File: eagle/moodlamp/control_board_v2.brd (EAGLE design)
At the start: 49.5 x 40 mm, 43 parts, among them IC1 MEGA8-AI, J1 POWER_JACKPTH, Q1 N-HEXFET-2D_SOT232-IRLL014N, Q2 N-HEXFET-2D_SOT232-IRLL014N, Q3 N-HEXFET-2D_SOT232-IRLL014N

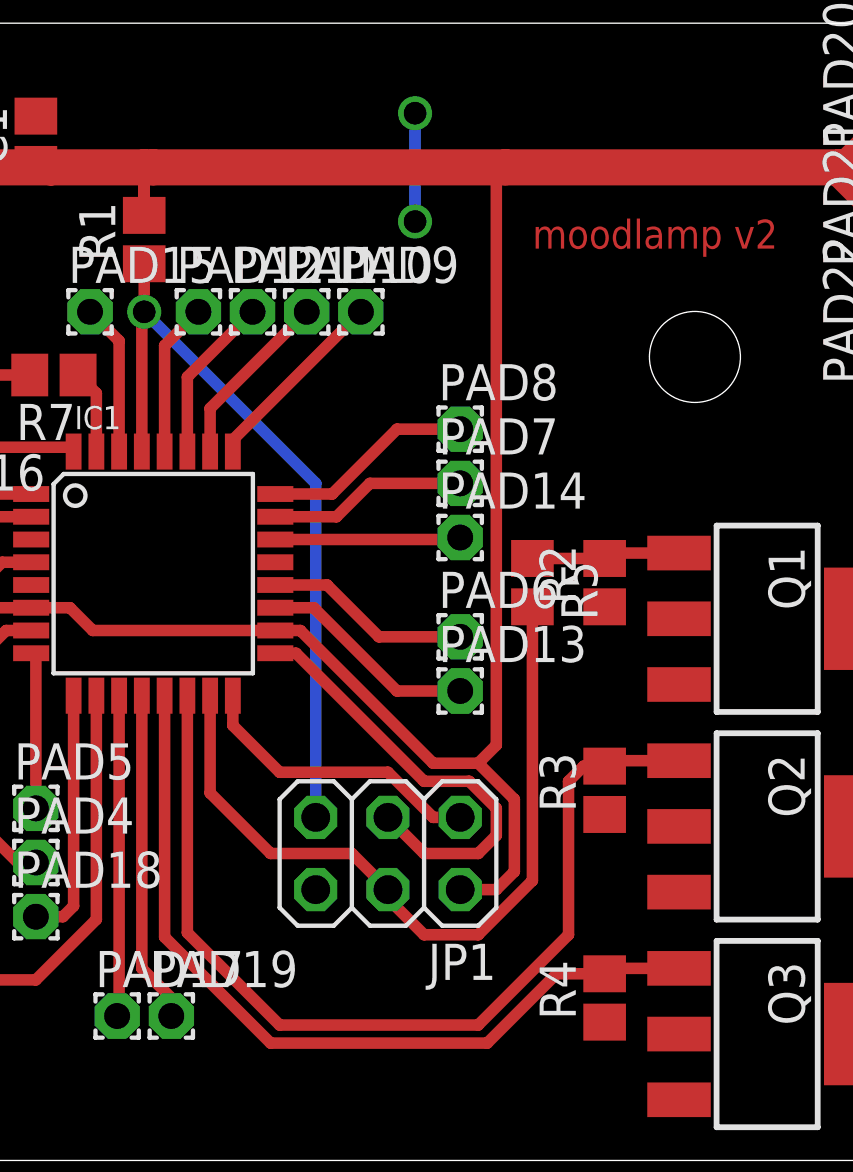
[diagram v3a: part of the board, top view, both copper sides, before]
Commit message: isp connector orientation fixed
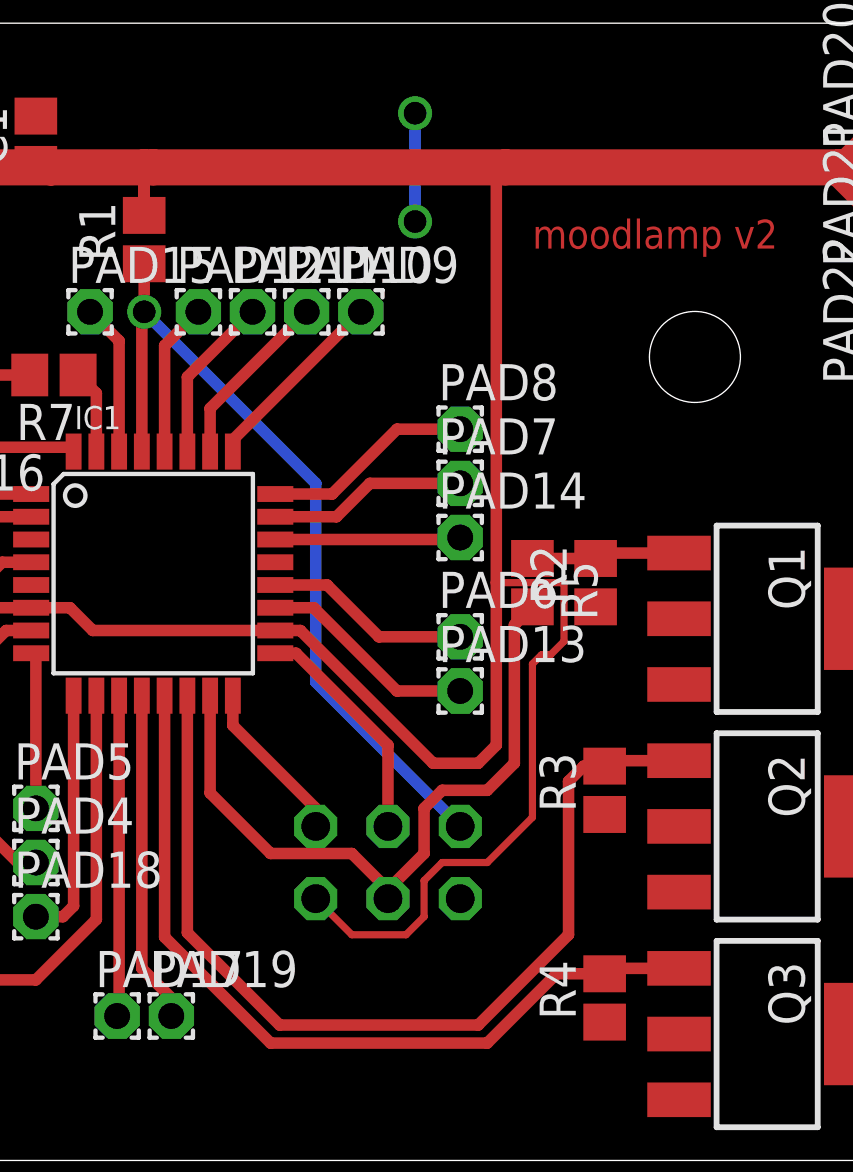
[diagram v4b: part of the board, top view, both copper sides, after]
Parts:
- moved R2 0.32 mm to (35.2, 20.3)
- moved JP1 0.32 mm to (27.9, 10.5), flipped to the bottom
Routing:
- net VCC: track 113.6 -> 129.0 mm
- net N$13: track 15.6 -> 8.16 mm
- net N$1: track 10.4 -> 5.80 mm
- net N$2: track 27.4 -> 24.4 mm
- net RST: track 27.0 -> 29.5 mm
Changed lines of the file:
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@@
 <element name="PAD1" library="wirepad" package="2,54/1,0" value="" x="47.625" y="19.05"/>
 <element name="Q1" library="transistor-power" package="SOT223" value="N-HEXFET-2D_SOT232-IRLL014N" x="41.275" y="19.05" rot="R270"/>
-<element name="R2" library="resistor" package="R0805" value="" x="35.56" y="20.32" rot="R90"/>
+<element name="R2" library="resistor" package="R0805" value="" x="35.2425" y="20.32" rot="R90"/>
 <element name="PAD2" library="wirepad" package="2,54/1,0" value="" x="47.625" y="11.7475"/>
 <element name="Q2" library="transistor-power" package="SOT223" value="N-HEXFET-2D_SOT232-IRLL014N" x="41.275" y="11.7475" rot="R270"/>
@@
 <element name="S2" library="switch" package="SKHMPXE010" value="SKHMPSE010" x="5.715" y="4.1275" rot="R180"/>
 <element name="USB1" library="usb_con-update" package="MOLEX-47364-0001" value="MOLEX-47346-0001" x="1.27" y="20.955"/>
-<element name="JP1" library="pinhead" package="2X03" value="" x="27.94" y="10.795" rot="R180"/>
+<element name="JP1" library="pinhead" package="2X03" value="" x="27.94" y="10.4775" rot="MR180"/>
 <element name="PAD4" library="wirepad" package="1,6/0,9" value="" x="15.5575" y="10.4775"/>
 <element name="PAD5" library="wirepad" package="1,6/0,9" value="" x="15.5575" y="12.3825"/>
@@
 <wire x1="24.86" y1="18.6375" x2="29.5275" y2="13.97" width="0.4064" layer="1"/>
 <wire x1="29.5275" y1="13.97" x2="31.115" y2="13.97" width="0.4064" layer="1"/>
-<wire x1="31.115" y1="13.97" x2="32.385" y2="12.7" width="0.4064" layer="1"/>
-<wire x1="32.385" y1="12.7" x2="32.385" y2="10.16" width="0.4064" layer="1"/>
-<wire x1="32.385" y1="10.16" x2="31.75" y2="9.525" width="0.4064" layer="1"/>
-<wire x1="31.75" y1="9.525" x2="30.48" y2="9.525" width="0.4064" layer="1"/>
 <wire x1="15.3924" y1="19.4375" x2="13.97" y2="19.4375" width="0.4064" layer="1"/>
 <wire x1="13.97" y1="19.4375" x2="13.32125" y2="19.4375" width="0.4064" layer="1"/>
@@
 <wire x1="19.3675" y1="34.925" x2="32.0675" y2="34.925" width="0.4064" layer="1"/>
 <wire x1="32.0675" y1="34.925" x2="31.75" y2="34.6075" width="0.4064" layer="1"/>
-<wire x1="31.75" y1="34.6075" x2="31.75" y2="14.605" width="0.4064" layer="1"/>
+<wire x1="31.75" y1="34.6075" x2="31.75" y2="20.32" width="0.4064" layer="1"/>
+<wire x1="31.75" y1="20.32" x2="31.75" y2="14.605" width="0.4064" layer="1"/>
 <wire x1="31.75" y1="14.605" x2="31.115" y2="13.97" width="0.4064" layer="1"/>
 <wire x1="13.335" y1="34.925" x2="11.1125" y2="32.7025" width="1.27" layer="1"/>
@@
 <wire x1="15.5575" y1="35.0275" x2="16.09" y2="34.925" width="1.27" layer="1"/>
 <wire x1="16.09" y1="34.925" x2="13.335" y2="34.925" width="1.27" layer="1"/>
+<wire x1="33.655" y1="17.78" x2="34.13125" y2="18.25625" width="0.254" layer="1"/>
+<wire x1="34.13125" y1="18.25625" x2="34.13125" y2="20.32" width="0.254" layer="1"/>
+<wire x1="34.13125" y1="20.32" x2="31.75" y2="20.32" width="0.254" layer="1"/>
+<wire x1="33.655" y1="17.78" x2="33.3375" y2="17.78" width="0.254" layer="1"/>
+<wire x1="33.3375" y1="17.78" x2="33.02" y2="17.4625" width="0.254" layer="1"/>
+<wire x1="33.02" y1="17.4625" x2="33.02" y2="12.065" width="0.254" layer="1"/>
+<wire x1="33.02" y1="12.065" x2="31.4325" y2="10.4775" width="0.254" layer="1"/>
+<wire x1="31.4325" y1="10.4775" x2="29.845" y2="10.4775" width="0.254" layer="1"/>
+<wire x1="29.845" y1="10.4775" x2="29.21" y2="9.8425" width="0.254" layer="1"/>
+<wire x1="29.21" y1="9.8425" x2="29.21" y2="8.5725" width="0.254" layer="1"/>
+<wire x1="29.21" y1="8.5725" x2="28.575" y2="7.9375" width="0.254" layer="1"/>
+<wire x1="28.575" y1="7.9375" x2="26.67" y2="7.9375" width="0.254" layer="1"/>
+<wire x1="26.67" y1="7.9375" x2="25.4" y2="9.2075" width="0.254" layer="1"/>
 </signal>
 <signal name="RST">
@@
 <contactref element="JP1" pad="5"/>
 <wire x1="19.285" y1="31.4525" x2="19.3675" y2="31.535" width="0.4064" layer="1"/>
-<wire x1="25.4" y1="12.065" x2="25.4" y2="23.8125" width="0.4064" layer="16"/>
 <wire x1="25.4" y1="23.8125" x2="19.3675" y2="29.845" width="0.4064" layer="16"/>
 <via x="19.3675" y="29.845" extent="1-16" drill="0.8"/>
@@
 <wire x1="19.285" y1="24.9301" x2="19.285" y2="29.7625" width="0.4064" layer="1"/>
 <wire x1="19.285" y1="29.7625" x2="19.3675" y2="29.845" width="0.4064" layer="1"/>
+<wire x1="30.48" y1="11.7475" x2="25.4" y2="16.8275" width="0.4064" layer="16"/>
+<wire x1="25.4" y1="16.8275" x2="25.4" y2="23.8125" width="0.4064" layer="16"/>
 </signal>
 <signal name="N$2">
@@
 <contactref element="R5" pad="2"/>
 <contactref element="JP1" pad="4"/>
-<wire x1="33.02" y1="9.8425" x2="33.02" y2="19.47" width="0.4064" layer="1"/>
-<wire x1="27.94" y1="9.525" x2="27.94" y2="9.2075" width="0.4064" layer="1"/>
-<wire x1="27.94" y1="9.2075" x2="29.21" y2="7.9375" width="0.4064" layer="1"/>
-<wire x1="29.21" y1="7.9375" x2="31.115" y2="7.9375" width="0.4064" layer="1"/>
-<wire x1="31.115" y1="7.9375" x2="33.02" y2="9.8425" width="0.4064" layer="1"/>
 <wire x1="23.8125" y1="10.795" x2="26.67" y2="10.795" width="0.4064" layer="1"/>
-<wire x1="26.67" y1="10.795" x2="27.94" y2="9.525" width="0.4064" layer="1"/>
 <wire x1="21.685" y1="16.3449" x2="21.685" y2="12.9225" width="0.4064" layer="1"/>
 <wire x1="21.685" y1="12.9225" x2="23.8125" y2="10.795" width="0.4064" layer="1"/>
+<wire x1="26.67" y1="10.795" x2="27.94" y2="9.525" width="0.4064" layer="1"/>
+<wire x1="27.94" y1="9.2075" x2="27.94" y2="9.525" width="0.4064" layer="1"/>
+<wire x1="27.94" y1="9.525" x2="29.21" y2="10.795" width="0.4064" layer="1"/>
+<wire x1="29.21" y1="10.795" x2="29.21" y2="12.3825" width="0.4064" layer="1"/>
+<wire x1="29.21" y1="12.3825" x2="29.845" y2="13.0175" width="0.4064" layer="1"/>
+<wire x1="29.845" y1="13.0175" x2="31.4325" y2="13.0175" width="0.4064" layer="1"/>
+<wire x1="31.4325" y1="13.0175" x2="32.385" y2="13.97" width="0.4064" layer="1"/>
+<wire x1="32.385" y1="13.97" x2="32.385" y2="18.835" width="0.4064" layer="1"/>
+<wire x1="32.385" y1="18.835" x2="33.02" y2="19.47" width="0.4064" layer="1"/>
 </signal>
 <signal name="N$3">
@@
 <contactref element="Q1" pad="1"/>
 <contactref element="R5" pad="1"/>
-<wire x1="33.02" y1="21.17" x2="35.56" y2="21.17" width="0.4064" layer="1"/>
-<wire x1="35.56" y1="21.17" x2="35.751" y2="21.361" width="0.4064" layer="1"/>
+<wire x1="33.02" y1="21.17" x2="35.2425" y2="21.17" width="0.4064" layer="1"/>
+<wire x1="35.2425" y1="21.17" x2="35.751" y2="21.361" width="0.4064" layer="1"/>
 <wire x1="35.751" y1="21.361" x2="38.176" y2="21.361" width="0.4064" layer="1"/>
 </signal>
@@
 <contactref element="JP1" pad="3"/>
 <wire x1="23.9776" y1="17.8375" x2="24.7075" y2="17.8375" width="0.4064" layer="1"/>
-<wire x1="24.7075" y1="17.8375" x2="29.21" y2="13.335" width="0.4064" layer="1"/>
-<wire x1="29.21" y1="13.335" x2="30.7975" y2="13.335" width="0.4064" layer="1"/>
-<wire x1="30.7975" y1="13.335" x2="31.75" y2="12.3825" width="0.4064" layer="1"/>
-<wire x1="27.94" y1="12.065" x2="29.21" y2="10.795" width="0.4064" layer="1"/>
-<wire x1="29.21" y1="10.795" x2="31.115" y2="10.795" width="0.4064" layer="1"/>
-<wire x1="31.115" y1="10.795" x2="31.75" y2="11.43" width="0.4064" layer="1"/>
-<wire x1="31.75" y1="11.43" x2="31.75" y2="12.3825" width="0.4064" layer="1"/>
+<wire x1="24.7075" y1="17.8375" x2="27.94" y2="14.605" width="0.4064" layer="1"/>
+<wire x1="27.94" y1="11.7475" x2="27.94" y2="14.605" width="0.4064" layer="1"/>
 </signal>
 <signal name="N$1">
 <contactref element="JP1" pad="1"/>
 <contactref element="IC1" pad="16"/>
-<wire x1="27.94" y1="13.6525" x2="29.5275" y2="12.065" width="0.4064" layer="1"/>
-<wire x1="29.5275" y1="12.065" x2="30.48" y2="12.065" width="0.4064" layer="1"/>
 <wire x1="22.485" y1="16.3449" x2="22.485" y2="15.2975" width="0.4064" layer="1"/>
-<wire x1="22.485" y1="15.2975" x2="24.13" y2="13.6525" width="0.4064" layer="1"/>
-<wire x1="24.13" y1="13.6525" x2="27.94" y2="13.6525" width="0.4064" layer="1"/>
+<wire x1="22.485" y1="15.2975" x2="25.4" y2="12.3825" width="0.4064" layer="1"/>
+<wire x1="25.4" y1="12.3825" x2="25.4" y2="11.7475" width="0.4064" layer="1"/>
 </signal>
 <signal name="N$14">

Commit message: drc cleanup
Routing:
- net VCC: track 129.0 -> 134.1 mm, vias 0 -> 2
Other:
- board text removed: "moodlamp v2"
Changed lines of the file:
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@@
 <hole x="6.985" y="17.4625" drill="3.2"/>
 <hole x="38.735" y="28.2575" drill="3.2"/>
-<text x="33.02" y="32.0675" size="1.016" layer="1" font="vector">moodlamp v2</text>
 <text x="-17.145" y="28.575" size="0.6096" layer="48">tohle je moc blizko u sebe -&gt;</text>
 </plain>
@@
 </class>
 </classes>
-<designrules name="default">
+<designrules name="Fusion_eagle_rule_v1.1">
 <description language="de">&lt;b&gt;EAGLE Design Rules&lt;/b&gt;
 &lt;p&gt;
@@
 <wire x1="19.3675" y1="34.925" x2="32.0675" y2="34.925" width="0.4064" layer="1"/>
 <wire x1="32.0675" y1="34.925" x2="31.75" y2="34.6075" width="0.4064" layer="1"/>
-<wire x1="31.75" y1="34.6075" x2="31.75" y2="20.32" width="0.4064" layer="1"/>
-<wire x1="31.75" y1="20.32" x2="31.75" y2="14.605" width="0.4064" layer="1"/>
+<wire x1="31.75" y1="34.6075" x2="31.75" y2="25.4" width="0.4064" layer="1"/>
+<wire x1="31.75" y1="25.4" x2="31.75" y2="14.605" width="0.4064" layer="1"/>
 <wire x1="31.75" y1="14.605" x2="31.115" y2="13.97" width="0.4064" layer="1"/>
 <wire x1="13.335" y1="34.925" x2="11.1125" y2="32.7025" width="1.27" layer="1"/>
@@
 <wire x1="15.5575" y1="35.0275" x2="16.09" y2="34.925" width="1.27" layer="1"/>
 <wire x1="16.09" y1="34.925" x2="13.335" y2="34.925" width="1.27" layer="1"/>
-<wire x1="33.655" y1="17.78" x2="34.13125" y2="18.25625" width="0.254" layer="1"/>
-<wire x1="34.13125" y1="18.25625" x2="34.13125" y2="20.32" width="0.254" layer="1"/>
-<wire x1="34.13125" y1="20.32" x2="31.75" y2="20.32" width="0.254" layer="1"/>
-<wire x1="33.655" y1="17.78" x2="33.3375" y2="17.78" width="0.254" layer="1"/>
-<wire x1="33.3375" y1="17.78" x2="33.02" y2="17.4625" width="0.254" layer="1"/>
-<wire x1="33.02" y1="17.4625" x2="33.02" y2="12.065" width="0.254" layer="1"/>
 <wire x1="33.02" y1="12.065" x2="31.4325" y2="10.4775" width="0.254" layer="1"/>
 <wire x1="31.4325" y1="10.4775" x2="29.845" y2="10.4775" width="0.254" layer="1"/>
@@
 <wire x1="28.575" y1="7.9375" x2="26.67" y2="7.9375" width="0.254" layer="1"/>
 <wire x1="26.67" y1="7.9375" x2="25.4" y2="9.2075" width="0.254" layer="1"/>
+<wire x1="33.02" y1="12.065" x2="33.02" y2="15.24" width="0.254" layer="1"/>
+<wire x1="33.02" y1="15.24" x2="34.29" y2="16.51" width="0.254" layer="1"/>
+<via x="34.29" y="16.51" extent="1-16" drill="0.6"/>
+<wire x1="34.29" y1="16.51" x2="34.29" y2="25.4" width="0.254" layer="16"/>
+<via x="34.29" y="25.4" extent="1-16" drill="0.6"/>
+<wire x1="34.29" y1="25.4" x2="31.75" y2="25.4" width="0.254" layer="1"/>
 </signal>
 <signal name="RST">
@@
 <contactref element="R5" pad="2"/>
 <contactref element="JP1" pad="4"/>
-<wire x1="23.8125" y1="10.795" x2="26.67" y2="10.795" width="0.4064" layer="1"/>
 <wire x1="21.685" y1="16.3449" x2="21.685" y2="12.9225" width="0.4064" layer="1"/>
-<wire x1="21.685" y1="12.9225" x2="23.8125" y2="10.795" width="0.4064" layer="1"/>
-<wire x1="26.67" y1="10.795" x2="27.94" y2="9.525" width="0.4064" layer="1"/>
+<wire x1="21.685" y1="12.9225" x2="24.13" y2="10.4775" width="0.4064" layer="1"/>
 <wire x1="27.94" y1="9.2075" x2="27.94" y2="9.525" width="0.4064" layer="1"/>
 <wire x1="27.94" y1="9.525" x2="29.21" y2="10.795" width="0.4064" layer="1"/>
@@
 <wire x1="32.385" y1="13.97" x2="32.385" y2="18.835" width="0.4064" layer="1"/>
 <wire x1="32.385" y1="18.835" x2="33.02" y2="19.47" width="0.4064" layer="1"/>
+<wire x1="24.13" y1="10.4775" x2="26.67" y2="10.4775" width="0.4064" layer="1"/>
+<wire x1="26.67" y1="10.4775" x2="27.94" y2="9.2075" width="0.4064" layer="1"/>
 </signal>
 <signal name="N$3">

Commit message: Silkscreen
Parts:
- removed USB1: MOLEX-47346-0001, usb_con-update:MOLEX-47364-0001
- added USB: MOLEX-47346-0001, usb_con-update:MOLEX-47364-0001
- PAD20, PAD21, PAD22: value (none) -> LED+
- renumbered JP1 to ISP, PAD1 to RED, PAD16 to P16, PAD2 to GRN, PAD3 to BLU, Q1 to T1, Q2 to T2, Q3 to T3
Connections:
- net +5V: now also USB.1; no longer USB1.1
- net GND: now also USB.5, USB.GND1, USB.GND2, USB.GND3, USB.GND4; no longer USB1.5, USB1.GND1, USB1.GND2, USB1.GND3, USB1.GND4
- net N$30: now also USB.2; no longer USB1.2
- net N$31: now also USB.3; no longer USB1.3
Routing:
- net N$3: track 3.25 -> 18.6 mm, vias 0 -> 1
- net N$7: track 3.25 -> 18.6 mm, vias 0 -> 1
- net N$5: track 3.57 -> 18.9 mm, vias 0 -> 1
- net N$31: track 10.7 -> 11.3 mm
- net N$30: track 19.3 -> 19.9 mm
- net +5V: track 8.54 -> 9.18 mm
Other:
- board text added: "LED+"
- board text added: "brmlab"
- board text added: "by Nephirus"
- board text added: "hackerspace prague"
- board text added: "http://nephirus.cz/moodlamp"
- board text added: "moodlamp v2"
- board text added: "order #XXXXXa"
- board text added: "rev 01"
- board text removed: "tohle je moc blizko u sebe ->"
